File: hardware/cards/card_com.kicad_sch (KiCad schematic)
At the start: 20 parts, among them J1 DE9_Pins, J2 Conn_01x03, J3 Conn_01x04, U1 16550, U2 MAX3241, U3 74HCT04, U4 74HCT08, U5 74HCT08, U6 74HCT125

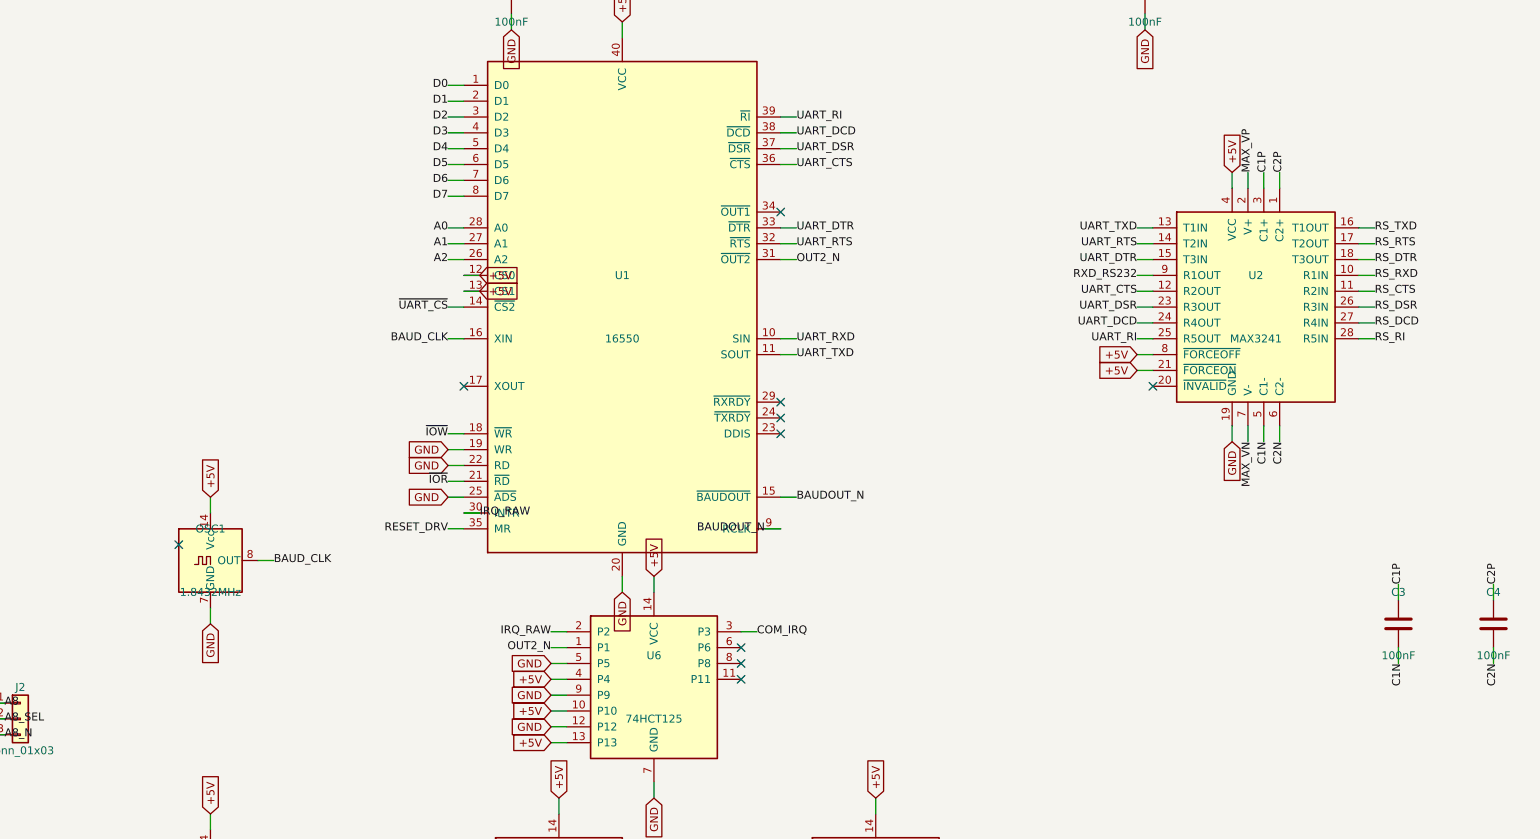
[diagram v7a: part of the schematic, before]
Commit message: JLCPCB sourcing pass: verify pinouts, LCSC part numbers, SMD build
Custom-symbol verification (open-questions Q5 resolved):
- MAX3241 symbol was wrong on nearly every pin and used MAX3243-style
  control names; regenerated to the real SSOP-28 pinout (SHDN#/EN#/
  R1OUTB/R2OUTB) and com_port rewired -- EN# must be GROUNDED (the old
  ~FORCEON-high would have disabled the receivers on real silicon)
- DS12C887 symbol wrong on 4 pins (DS=17, RESET#=18, IRQ#=19, SQW=23)

Sourcing (every part checked against the JLC DB; ~45 line items):
- New tools/parts.py maps (lib_id, value) -> LCSC; build.py applies it as
  an 'LCSC Part Num' property on every component (384 across the project)
- Sheets stay generic; stock-forced substitutions bound in the map:
  '374->'574 (parallel rewired), '163->'161, '157->HC157 (+HCT-buffered
  3.3V selects, I0/I1 swapped), '02->HC02, TCM809->MCP809, 2N3904->MMBT3904
- bus_mcu address counters moved to the 3.3V domain (HC161 on 3V3_BUS,
  loaded from MCU-side MD0-7; HCT244s read the 3.3V outputs at TTL Vih)
- 14.318 XOs are 3.3V-only parts: powered from 3V3, squared up via spare
  HCT gates (cpu_core U13, card_isatest U19)
- COM baud reference is now a 1.8432MHz crystal on the 16C550's XIN/XOUT
  (3.3V-only oscillators vs a 5V-only soft card)
- Supervisor QSPI header replaced with a real W25Q128JVSIQ
- Socket policy (fab installs sockets): V20 DIP-40, SRAM DIP-32 (no 5V
  512Kx8 SRAM at JLC at all), DS12C887 DIP-24, female headers for modules

Docs: CLAUDE.md fabrication-constraints section (SMD, 100x100mm, generic-
symbols rule, voltage-domain rule); README + hardware/README fab notes;
notes/jlcpcb-sourcing.md (decisions, thin-stock flags, not-at-JLC list);
stale questions-sidecar.md collapsed to its supersession record.

Rebuilt motherboard + cards: structural ERC 0, byte-identical rebuilds.

Co-Authored-By: Claude Fable 5 <noreply@anthropic.com>
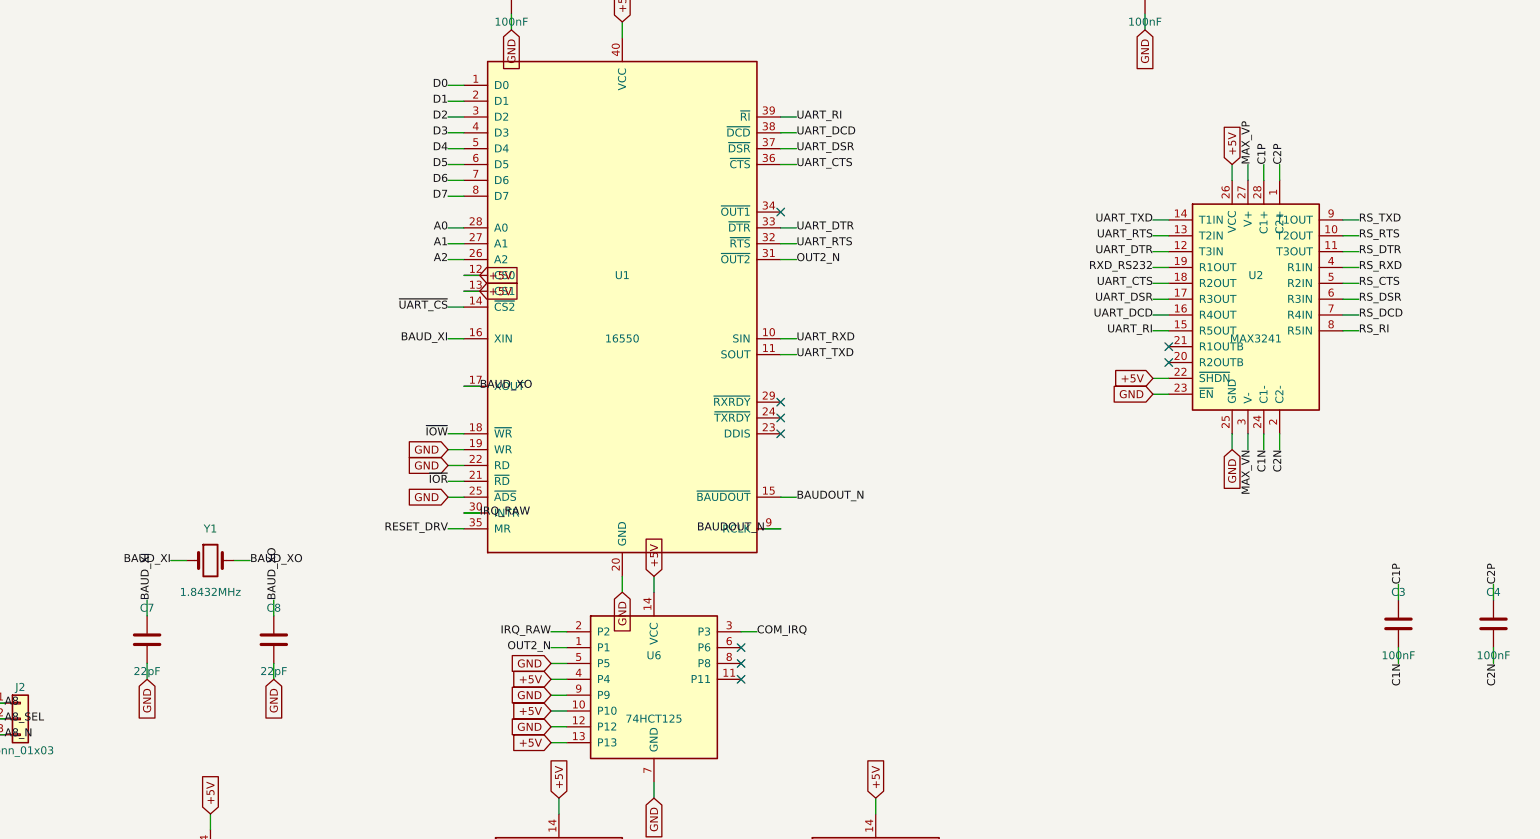
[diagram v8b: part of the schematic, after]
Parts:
- removed J3: Conn_01x04, symbol Connector_Generic:Conn_01x04
- removed OSC1: 1.8432MHz, symbol Oscillator:ACO-xxxMHz
- added C7, C8: 22pF, symbol Device:C
- added JP1: Conn_01x03, symbol Connector_Generic:Conn_01x03
- added Y1: 1.8432MHz, symbol Device:Crystal
- C1, C2, C3, C4, C5, C6: LCSC Part Num (none) -> C14663
- J1: LCSC Part Num (none) -> C141880
- J2, JP2: LCSC Part Num (none) -> C2337
- J3: renamed from JP1; value Conn_01x03 -> Conn_01x04; symbol Connector_Generic:Conn_01x03 -> Connector_Generic:Conn_01x04; LCSC Part Num (none) -> C2337
- J_IN, J_OUT: LCSC Part Num (none) -> C2333
- U1: LCSC Part Num (none) -> C544406
- U2: LCSC Part Num (none) -> C406859
- U3: LCSC Part Num (none) -> C672096
- U4, U5: LCSC Part Num (none) -> C5959
- U6: LCSC Part Num (none) -> C5962
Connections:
- net +5V: now also J3.4 (Pin_4), U2.22 (~{SHDN}), U2.26 (VCC); no longer U2.21 (~{FORCEON}), U2.4 (VCC), U2.8 (~{FORCEOFF})
- net C1N: now also U2.24 (C1-); no longer U2.5 (C1-)
- net C1P: now also U2.28 (C1+); no longer U2.3 (C1+)
- net C2N: now also U2.2 (C2-); no longer U2.6 (C2-)
- net CONSOLE_RXI: now also JP1.3 (Pin_3)
- net GND: now also J3.1 (Pin_1), U2.23 (~{EN}), U2.25 (GND), C7.2, C8.2; no longer U2.19 (GND)
- net MAX_VN: now also U2.3 (V-); no longer U2.7 (V-)
- net MAX_VP: now also U2.27 (V+); no longer U2.2 (V+)
- net RS_CTS: now also U2.5 (R2IN); no longer U2.11 (R2IN)
- net RS_DCD: now also U2.7 (R4IN); no longer U2.27 (R4IN)
- net RS_DSR: now also U2.6 (R3IN); no longer U2.26 (R3IN)
- net RS_DTR: now also U2.11 (T3OUT); no longer U2.18 (T3OUT)
- net RS_RI: now also U2.8 (R5IN); no longer U2.28 (R5IN)
- net RS_RTS: now also U2.10 (T2OUT); no longer U2.17 (T2OUT)
- net RS_RXD: now also U2.4 (R1IN); no longer U2.10 (R1IN)
- net RS_TXD: now also U2.9 (T1OUT); no longer U2.16 (T1OUT)
- net RXD_RS232: now also U2.19 (R1OUT), JP1.1 (Pin_1); no longer J3.1 (Pin_1), U2.9 (R1OUT)
- net UART_CTS: now also U2.18 (R2OUT); no longer U2.12 (R2OUT)
- net UART_DCD: now also U2.16 (R4OUT); no longer U2.24 (R4OUT)
- net UART_DSR: now also U2.17 (R3OUT); no longer U2.23 (R3OUT)
- net UART_DTR: now also U2.12 (T3IN); no longer U2.15 (T3IN)
- net UART_RI: now also U2.15 (R5OUT); no longer U2.25 (R5OUT)
- net UART_RTS: now also U2.13 (T2IN); no longer U2.14 (T2IN)
- net UART_RXD: now also JP1.2 (Pin_2); no longer J3.2 (Pin_2)
- net UART_TXD: now also J3.2 (Pin_2), U2.14 (T1IN); no longer U2.13 (T1IN)
- net BAUD_XO: now reaches U1.17 (XOUT)
- net BAUD_XO: now also C8.1, Y1.2
- net BAUD_CLK renamed BAUD_XI
- net BAUD_XI: now also C7.1, Y1.1
- no-connect marks 16 -> 15
